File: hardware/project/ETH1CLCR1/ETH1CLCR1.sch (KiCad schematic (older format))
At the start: 0 parts

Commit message: PCB layout
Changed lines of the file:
@@
 F1 "FGEN_Buffer.sch" 50
 F2 "FGEN" I R 3450 9500 50
-F3 "SR10CTR" I R 3450 9300 50
-F4 "SR100CTR" I R 3450 8900 50
-F5 "SR1KCTR" I R 3450 9100 50
-F6 "SR10KCTR" I R 3450 9200 50
+F3 "SR10CTR" I R 3450 9200 50
+F4 "SR100CTR" I R 3450 9300 50
+F5 "SR1KCTR" I R 3450 8900 50
+F6 "SR10KCTR" I R 3450 9100 50
 F7 "VLI" B L 2350 8400 50
 F8 "HCUR" O L 2350 8300 50
@@
 F11 "MCU3_MISO" I L 8850 8400 50
 F12 "MCU3_MOSI" O L 8850 8500 50
-F13 "SR1KCTR" O L 8850 7700 50
+F13 "SR1KCTR" O L 8850 7600 50
 F14 "SR10KCTR" O L 8850 7800 50
 F15 "SR10CTR" O L 8850 7900 50
@@
 F64 "DAC_DIN" O L 8850 3500 50
 F65 "DAC_SCLK" O L 8850 3600 50
-F66 "FB_CAP" O L 8850 7600 50
+F66 "FB_CAP" O L 8850 7700 50
 F67 "CXN_REL4" O R 10450 5300 50
 F68 "CXN_REL5" O R 10450 5400 50

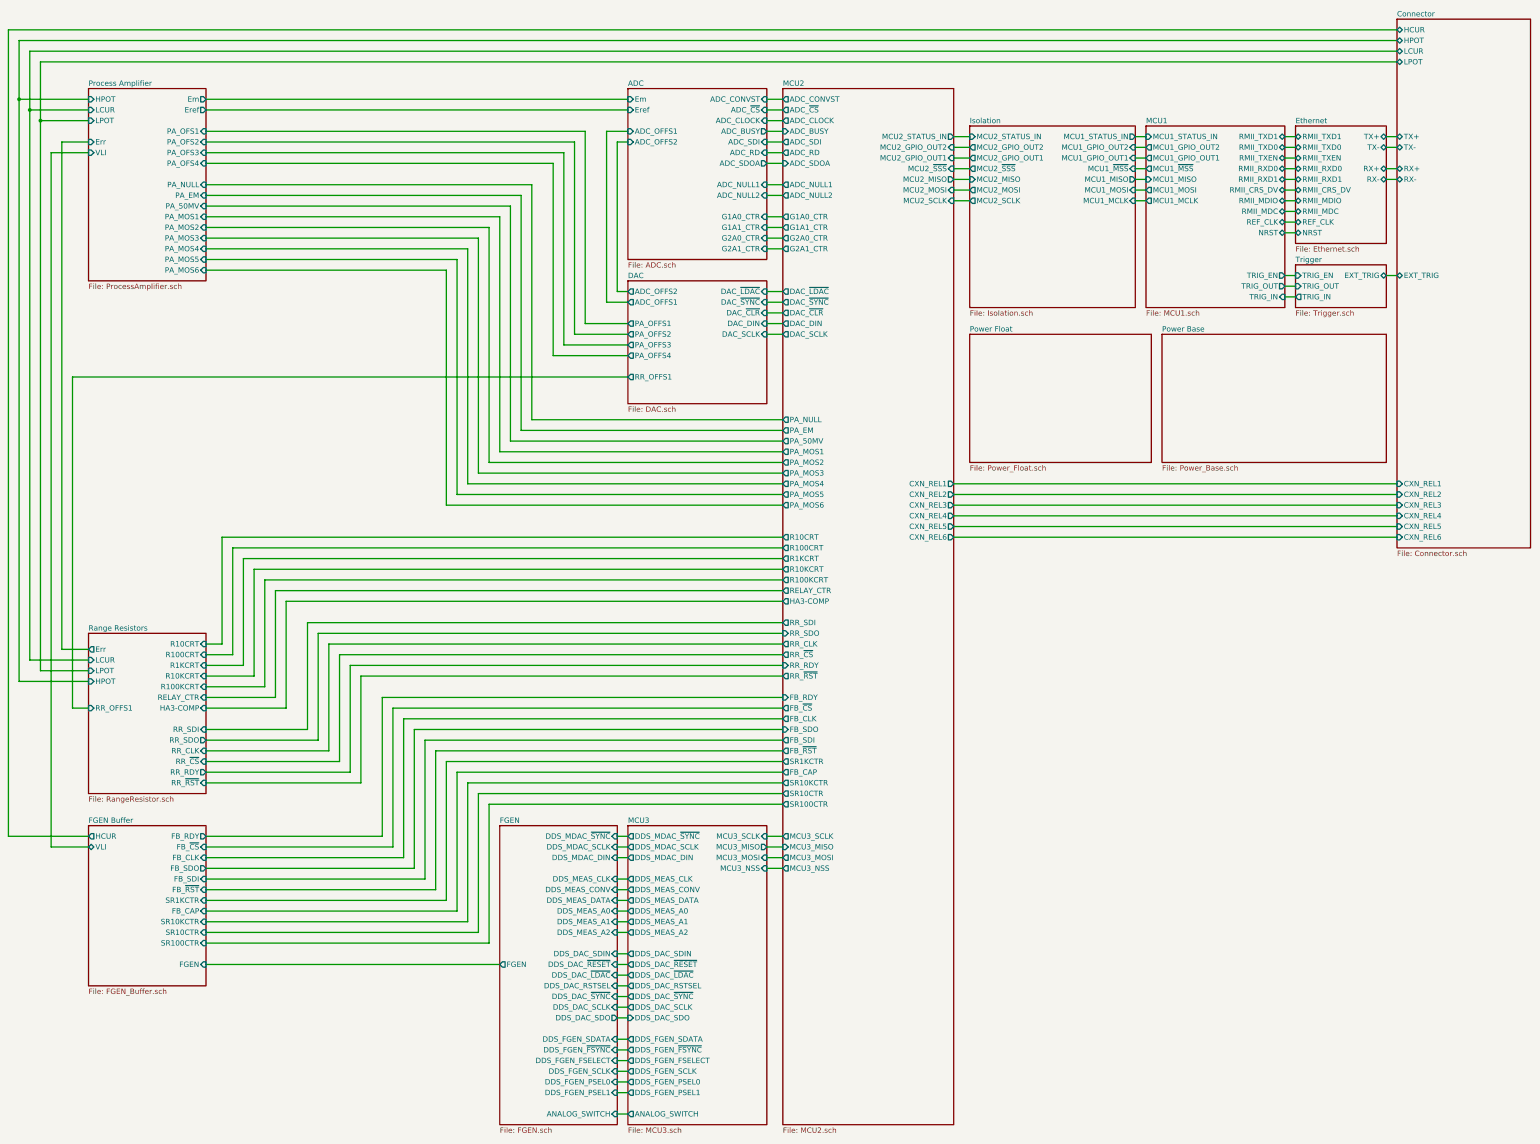
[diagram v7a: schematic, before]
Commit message: Redesigned the power supply, added humidy+temp. sensor.
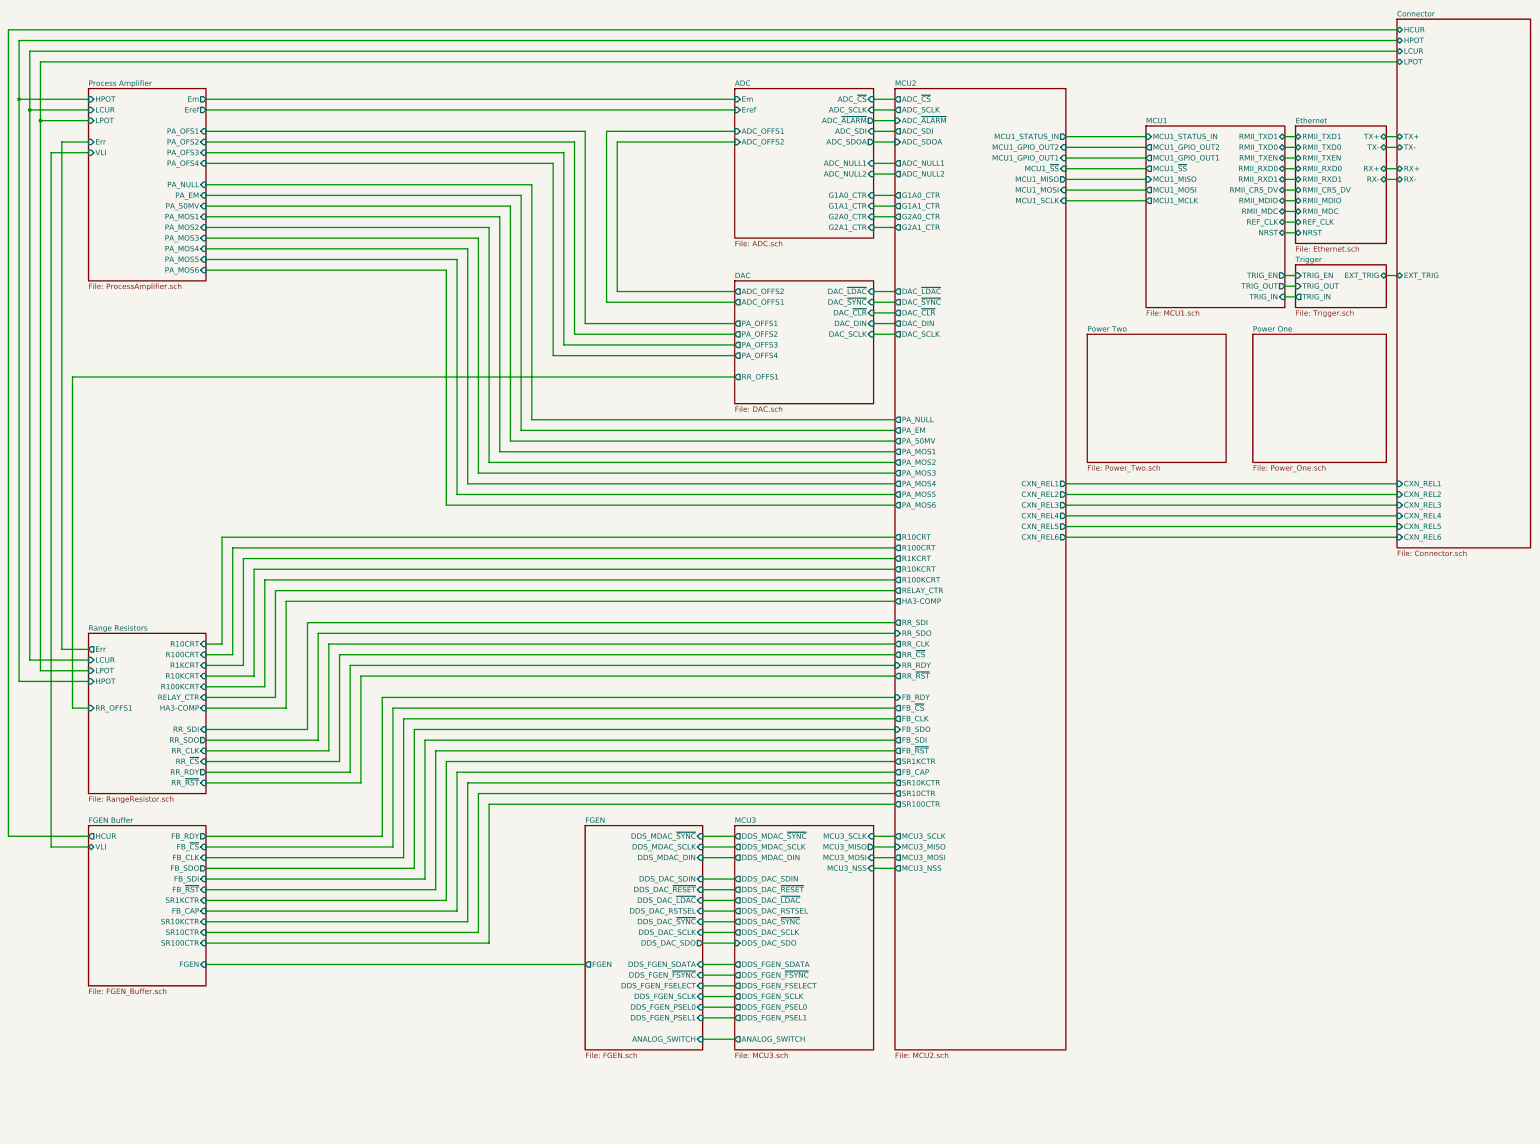
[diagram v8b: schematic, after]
